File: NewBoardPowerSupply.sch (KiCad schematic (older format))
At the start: 22 parts, among them IC201 ADM7172ACPZ-4.2-R7, IC202 LT1716CS5#TRPBF, IC203 ADM7154ARDZ-3.3-R7, IC204 IRF9358PBF, U201 LM4040EIM3X-2.5_NOPB

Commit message: added vishay dude & capacitor & resistor footprints
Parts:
- C201, C202, C203, C204, C205, C206, C207, C208, C209, C210, C211, C212: footprint (none) -> Capacitor_SMD:C_0402_1005Metric
- R201, R202, R203, R204: footprint (none) -> Resistor_SMD:R_0402_1005Metric
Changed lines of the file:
@@
 F 0 "C201" H 3915 5846 50  0000 L CNN
 F 1 "100u" H 3915 5755 50  0000 L CNN
-F 2 "" H 3838 5650 50  0001 C CNN
+F 2 "Capacitor_SMD:C_0402_1005Metric" H 3838 5650 50  0001 C CNN
 F 3 "~" H 3800 5800 50  0001 C CNN
 	1    3800 5800
@@
 F 0 "C202" H 6065 5696 50  0000 L CNN
 F 1 "100u" H 6065 5605 50  0000 L CNN
-F 2 "" H 5988 5500 50  0001 C CNN
+F 2 "Capacitor_SMD:C_0402_1005Metric" H 5988 5500 50  0001 C CNN
 F 3 "~" H 5950 5650 50  0001 C CNN
 	1    5950 5650
@@
 F 0 "C212" H 8515 5796 50  0000 L CNN
 F 1 "1u" H 8515 5705 50  0000 L CNN
-F 2 "" H 8438 5600 50  0001 C CNN
+F 2 "Capacitor_SMD:C_0402_1005Metric" H 8438 5600 50  0001 C CNN
 F 3 "~" H 8400 5750 50  0001 C CNN
 	1    8400 5750
@@
 F 0 "C209" H 8065 5796 50  0000 L CNN
 F 1 "100u" H 8065 5705 50  0000 L CNN
-F 2 "" H 7988 5600 50  0001 C CNN
+F 2 "Capacitor_SMD:C_0402_1005Metric" H 7988 5600 50  0001 C CNN
 F 3 "~" H 7950 5750 50  0001 C CNN
 	1    7950 5750
@@
 F 0 "C207" H 7865 5296 50  0000 L CNN
 F 1 "10u" H 7865 5205 50  0000 L CNN
-F 2 "" H 7788 5100 50  0001 C CNN
+F 2 "Capacitor_SMD:C_0402_1005Metric" H 7788 5100 50  0001 C CNN
 F 3 "~" H 7750 5250 50  0001 C CNN
 	1    7750 5250
@@
 F 0 "C203" H 6315 6046 50  0000 L CNN
 F 1 "1u" H 6315 5955 50  0000 L CNN
-F 2 "" H 6238 5850 50  0001 C CNN
+F 2 "Capacitor_SMD:C_0402_1005Metric" H 6238 5850 50  0001 C CNN
 F 3 "~" H 6200 6000 50  0001 C CNN
 	1    6200 6000
@@
 F 0 "C211" H 8265 5396 50  0000 L CNN
 F 1 "100u" H 8265 5305 50  0000 L CNN
-F 2 "" H 8188 5200 50  0001 C CNN
+F 2 "Capacitor_SMD:C_0402_1005Metric" H 8188 5200 50  0001 C CNN
 F 3 "~" H 8150 5350 50  0001 C CNN
 	1    8150 5350
@@
 F 0 "C204" H 7185 4654 50  0000 R CNN
 F 1 "100u" H 7185 4745 50  0000 R CNN
-F 2 "" H 7338 4550 50  0001 C CNN
+F 2 "Capacitor_SMD:C_0402_1005Metric" H 7338 4550 50  0001 C CNN
 F 3 "~" H 7300 4700 50  0001 C CNN
 	1    7300 4700
@@
 F 0 "R201" H 5570 1196 50  0000 L CNN
 F 1 "10k" H 5570 1105 50  0000 L CNN
-F 2 "" V 5430 1150 50  0001 C CNN
+F 2 "Resistor_SMD:R_0402_1005Metric" V 5430 1150 50  0001 C CNN
 F 3 "~" H 5500 1150 50  0001 C CNN
 	1    5500 1150
@@
 F 0 "R202" H 6170 1196 50  0000 L CNN
 F 1 "14k" H 6170 1105 50  0000 L CNN
-F 2 "" V 6030 1150 50  0001 C CNN
+F 2 "Resistor_SMD:R_0402_1005Metric" V 6030 1150 50  0001 C CNN
 F 3 "~" H 6100 1150 50  0001 C CNN
 	1    6100 1150
@@
 F 0 "R203" H 6170 2196 50  0000 L CNN
 F 1 "12k" H 6170 2105 50  0000 L CNN
-F 2 "" V 6030 2150 50  0001 C CNN
+F 2 "Resistor_SMD:R_0402_1005Metric" V 6030 2150 50  0001 C CNN
 F 3 "~" H 6100 2150 50  0001 C CNN
 	1    6100 2150
@@
 F 0 "C206" H 7865 1546 50  0000 L CNN
 F 1 "1u" H 7865 1455 50  0000 L CNN
-F 2 "" H 7788 1350 50  0001 C CNN
+F 2 "Capacitor_SMD:C_0402_1005Metric" H 7788 1350 50  0001 C CNN
 F 3 "~" H 7750 1500 50  0001 C CNN
 	1    7750 1500
@@
 F 0 "C210" H 8265 1546 50  0000 L CNN
 F 1 "0.1u" H 8265 1455 50  0000 L CNN
-F 2 "" H 8188 1350 50  0001 C CNN
+F 2 "Capacitor_SMD:C_0402_1005Metric" H 8188 1350 50  0001 C CNN
 F 3 "~" H 8150 1500 50  0001 C CNN
 	1    8150 1500
@@
 F 0 "C205" H 7715 2696 50  0000 L CNN
 F 1 "2.2u" H 7715 2605 50  0000 L CNN
-F 2 "" H 7638 2500 50  0001 C CNN
+F 2 "Capacitor_SMD:C_0402_1005Metric" H 7638 2500 50  0001 C CNN
 F 3 "~" H 7600 2650 50  0001 C CNN
 	1    7600 2650
@@
 F 0 "R204" H 6520 2496 50  0000 L CNN
 F 1 "47k" H 6520 2405 50  0000 L CNN
-F 2 "" V 6380 2450 50  0001 C CNN
+F 2 "Resistor_SMD:R_0402_1005Metric" V 6380 2450 50  0001 C CNN
 F 3 "~" H 6450 2450 50  0001 C CNN
 	1    6450 2450
@@
 F 0 "C208" H 7785 4654 50  0000 R CNN
 F 1 "100u" H 7785 4745 50  0000 R CNN
-F 2 "" H 7938 4550 50  0001 C CNN
+F 2 "Capacitor_SMD:C_0402_1005Metric" H 7938 4550 50  0001 C CNN
 F 3 "~" H 7900 4700 50  0001 C CNN
 	1    7900 4700

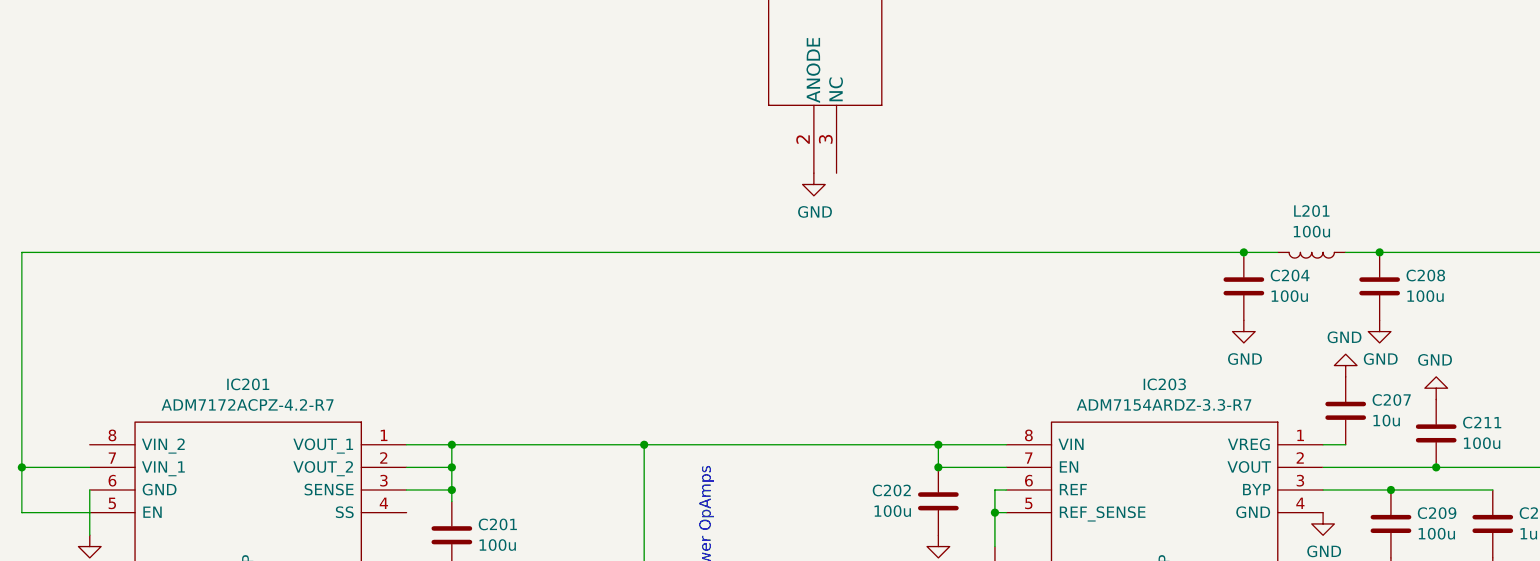
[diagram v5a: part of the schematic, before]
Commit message: add coil
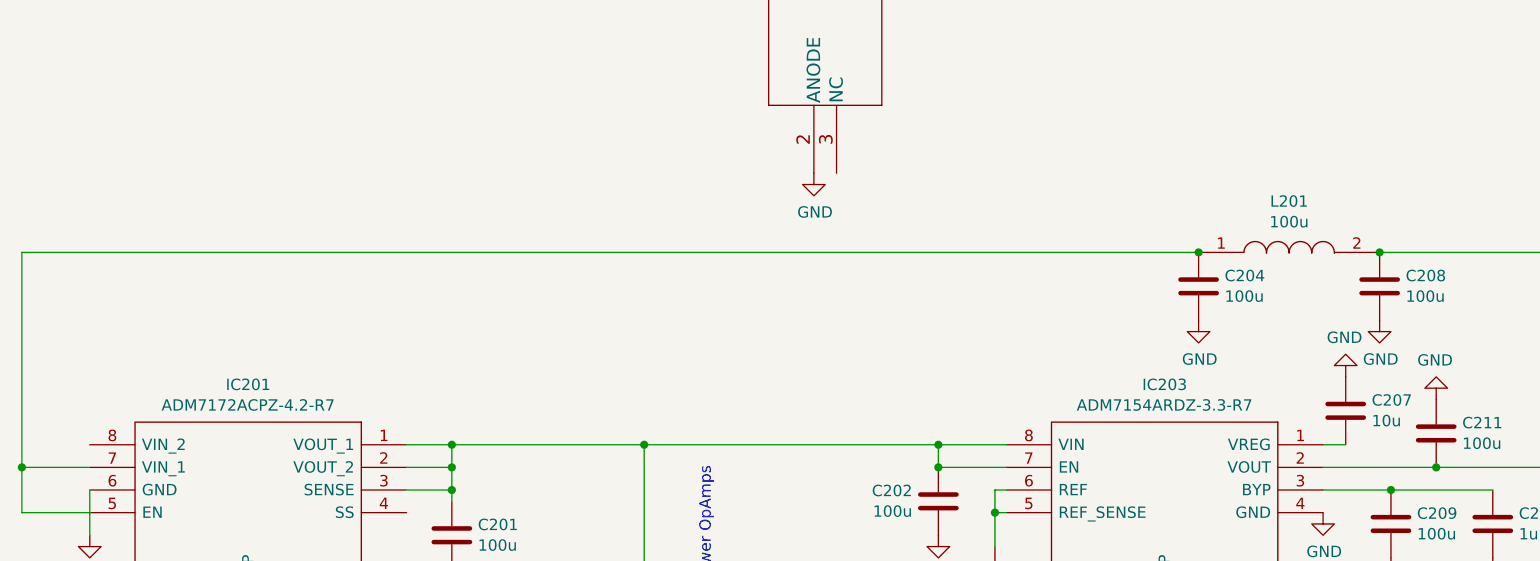
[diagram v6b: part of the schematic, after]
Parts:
- removed L201: 100u, symbol Device:L
- added L201: 100u, footprint libraries:7447714220, symbol 7447714101:7447714101
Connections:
- net goes_to_CPU_and_USBchip: now also L201.2
- net at C204.2, IC201.5 (EN), IC201.7 (VIN_1): now also L201.1
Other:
- moved on the sheet: C204
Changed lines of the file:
@@
 L Device:C C204
 U 1 1 60C3DCA3
-P 7300 4700
-F 0 "C204" H 7185 4654 50  0000 R CNN
-F 1 "100u" H 7185 4745 50  0000 R CNN
-F 2 "Capacitor_SMD:C_0402_1005Metric" H 7338 4550 50  0001 C CNN
-F 3 "~" H 7300 4700 50  0001 C CNN
-	1    7300 4700
+P 7100 4700
+F 0 "C204" H 6985 4654 50  0000 R CNN
+F 1 "100u" H 6985 4745 50  0000 R CNN
+F 2 "Capacitor_SMD:C_0402_1005Metric" H 7138 4550 50  0001 C CNN
+F 3 "~" H 7100 4700 50  0001 C CNN
+	1    7100 4700
 	-1   0    0    1
-$EndComp
-$Comp
-L Device:L L201
-U 1 1 60C3F9A3
-P 7600 4550
-F 0 "L201" V 7419 4550 50  0000 C CNN
-F 1 "100u" V 7510 4550 50  0000 C CNN
-F 2 "" H 7600 4550 50  0001 C CNN
-F 3 "~" H 7600 4550 50  0001 C CNN
-	1    7600 4550
-	0    1    1    0
 $EndComp
 $Comp
 L power:GND #PWR0209
 U 1 1 60C42E03
-P 7300 4850
-F 0 "#PWR0209" H 7300 4600 50  0001 C CNN
-F 1 "GND" H 7305 4677 50  0000 C CNN
-F 2 "" H 7300 4850 50  0001 C CNN
-F 3 "" H 7300 4850 50  0001 C CNN
-	1    7300 4850
+P 7100 4850
+F 0 "#PWR0209" H 7100 4600 50  0001 C CNN
+F 1 "GND" H 7105 4677 50  0000 C CNN
+F 2 "" H 7100 4850 50  0001 C CNN
+F 3 "" H 7100 4850 50  0001 C CNN
+	1    7100 4850
 	1    0    0    -1
 $EndComp
@@
 	1    0    0    -1
 $EndComp
-Wire Wire Line
-	7900 4550 7750 4550
-Wire Wire Line
-	7450 4550 7300 4550
-Wire Wire Line
-	7300 4550 1900 4550
-Connection ~ 7300 4550
-Connection ~ 7900 4550
 Connection ~ 1900 5500
 Wire Wire Line
@@
 Wire Wire Line
 	4650 5400 4650 7000
+$Comp
+L 7447714101:7447714101 L201
+U 1 1 60D14724
+P 7100 4550
+F 0 "L201" H 7500 4775 50  0000 C CNN
+F 1 "100u" H 7500 4684 50  0000 C CNN
+F 2 "footprint libraries:7447714220" H 7750 4600 50  0001 L CNN
+F 3 "" H 7750 4500 50  0001 L CNN
+F 4 "Wurth WE-PD Series Shielded Wire-wound SMD Inductor 100 uH +/-20% 1.5A Idc" H 7750 4400 50  0001 L CNN "Description"
+F 5 "5" H 7750 4300 50  0001 L CNN "Height"
+F 6 "Wurth Elektronik" H 7750 4200 50  0001 L CNN "Manufacturer_Name"
+F 7 "7447714101" H 7750 4100 50  0001 L CNN "Manufacturer_Part_Number"
+F 8 "710-7447714101" H 7750 4000 50  0001 L CNN "Mouser Part Number"
+F 9 "https://www.mouser.co.uk/ProductDetail/Wurth-Elektronik/7447714101?qs=XJfXErqHgA5R%252B3wMfRjrqw%3D%3D" H 7750 3900 50  0001 L CNN "Mouser Price/Stock"
+F 10 "" H 7750 3800 50  0001 L CNN "Arrow Part Number"
+F 11 "" H 7750 3700 50  0001 L CNN "Arrow Price/Stock"
+	1    7100 4550
+	1    0    0    -1
+$EndComp
+Connection ~ 7900 4550
+Wire Wire Line
+	1900 4550 7100 4550
+Connection ~ 7100 4550
 $EndSCHEMATC

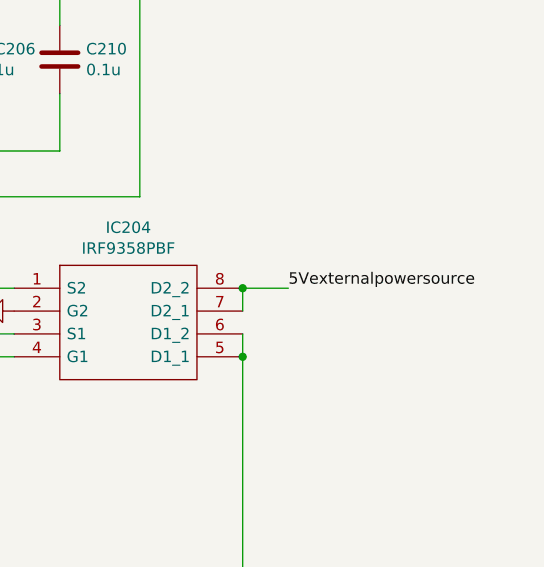
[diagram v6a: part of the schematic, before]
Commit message: added 5v power source 'ports'
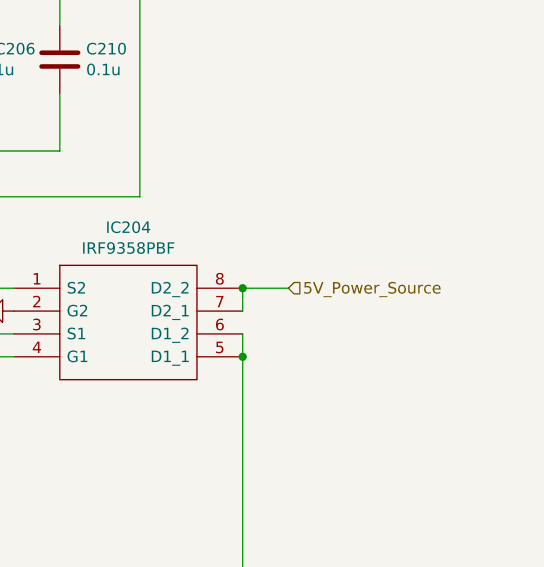
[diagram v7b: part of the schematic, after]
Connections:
- net 5Vexternalpowersource renamed 5V_Power_Source
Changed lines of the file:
@@
 	8950 2500 9150 2500
 Connection ~ 8950 2500
-Text Label 9150 2500 0    50   ~ 0
-5Vexternalpowersource
 Text Label 9050 3850 0    50   ~ 0
 goes_to_CPU_and_USBchip
@@
 	1900 4550 7100 4550
 Connection ~ 7100 4550
+Text HLabel 9150 2500 2    50   Input ~ 0
+5V_Power_Source
 $EndSCHEMATC

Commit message: pushing other ports
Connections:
- net 3.3V_rail renamed 3.3V_Supply
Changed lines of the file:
@@
 	8150 5500 8900 5500
 Connection ~ 8150 5500
-Text Label 8900 5500 0    50   ~ 0
-3.3V_rail
 Connection ~ 4650 5400
 Wire Wire Line
@@
 Text HLabel 9150 2500 2    50   Input ~ 0
 5V_Power_Source
+Text HLabel 8900 5500 2    50   Output ~ 0
+3.3V_Supply
 $EndSCHEMATC
